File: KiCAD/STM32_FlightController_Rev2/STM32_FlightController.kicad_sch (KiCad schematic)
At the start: 71 parts, among them J1 USB_B_Micro, J11 GPS_V_{IN}, J12 GPS_TX, J13 GND, J14 GPS_RX, J15 ELRS_V_{IN}, J16 GND, J17 ELRS_TX, J18 ELRS_RX, J19 Conn_02x05_Odd_Even, J2 GND, J3 BAT, J4 CRT, J5 5V, J6 S1, J7 S2, J8 S3, J9 S4, Q1 IRLML6244, Q2 IRLML6244, SW1 PTS815SJM, SW2 SW_SPDT, U1 USBLC6-2SC6, U2 AMS1117-3.3, U3 TLV70018, U4 STM32F405RGTx, U5 BMP390L, U6 ICM-20948, Y1 8MHz

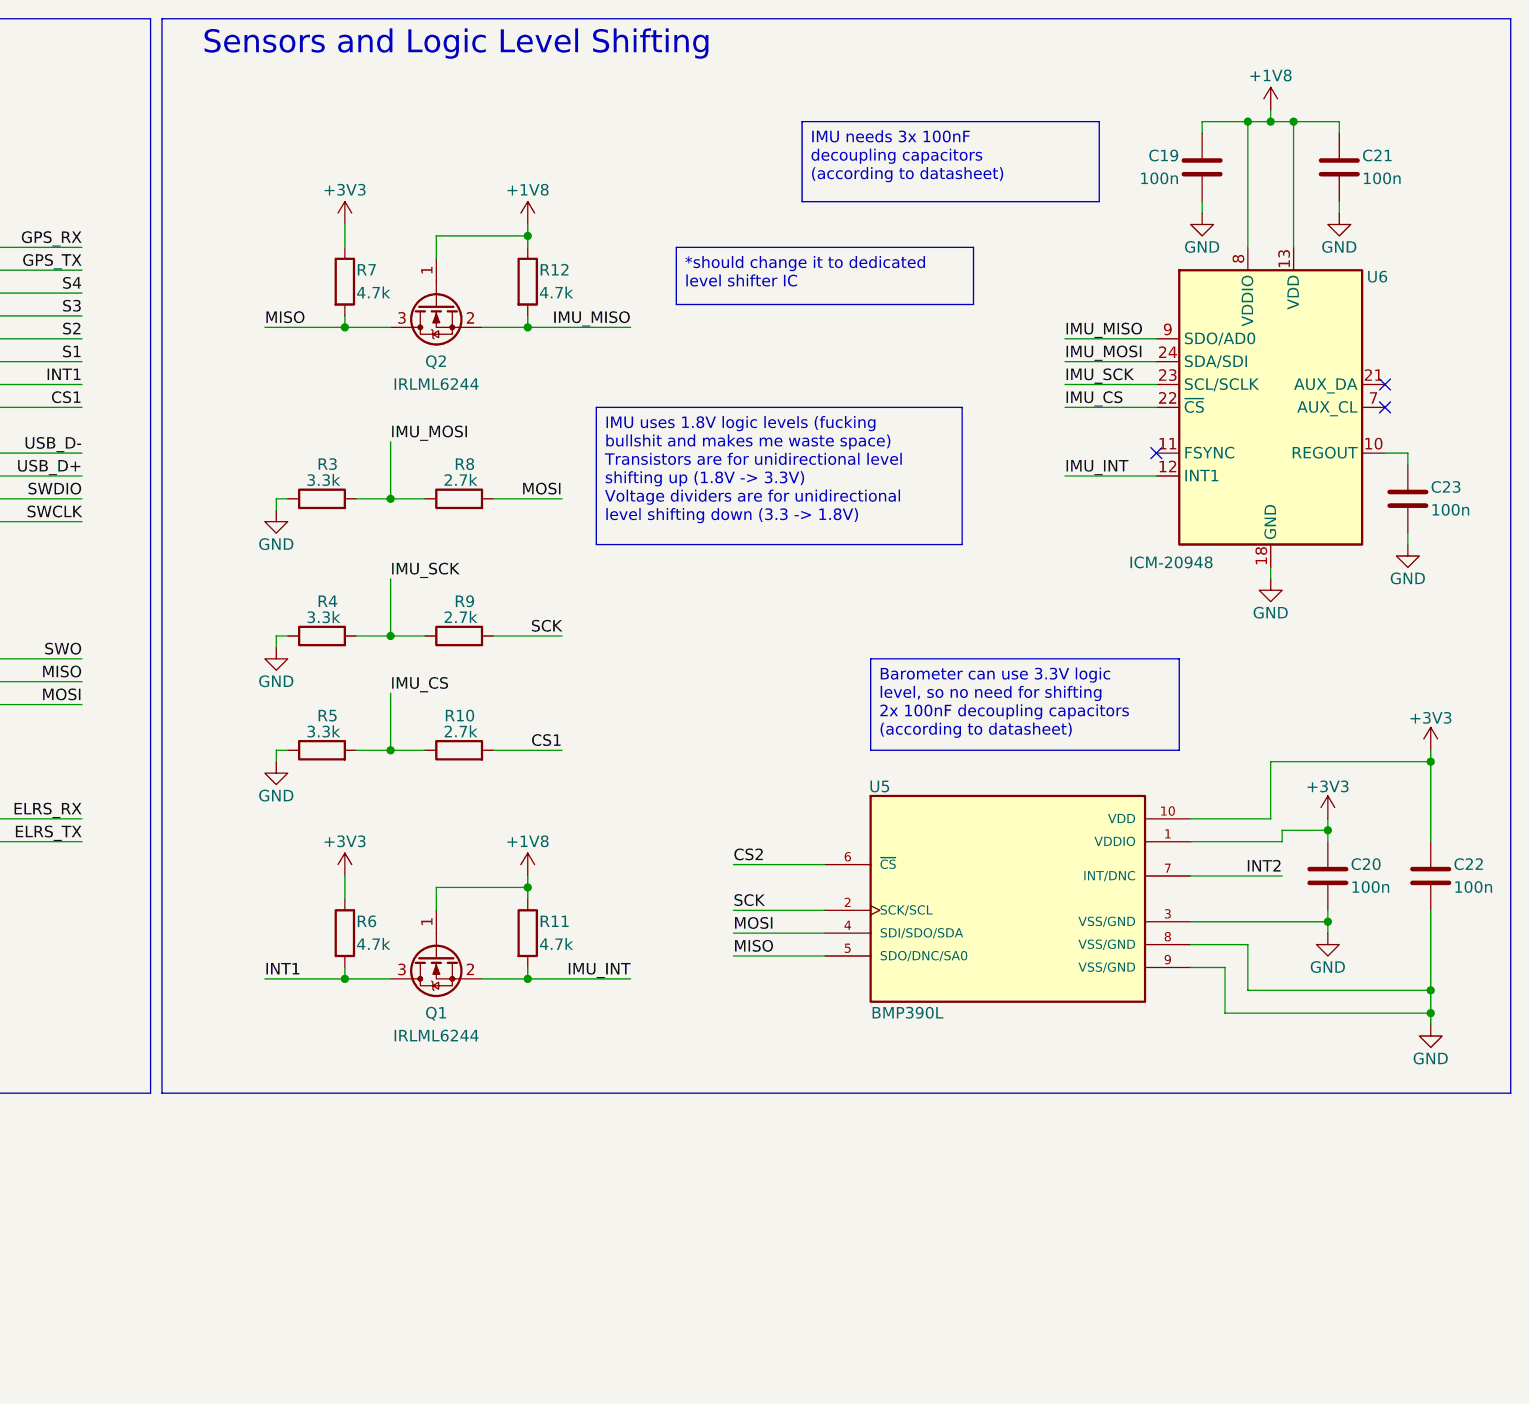
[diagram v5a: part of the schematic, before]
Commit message: replaced transistors with level shifter ICs
transistors appeared to switch to slowly for SPI, ICs seemed like they would be fast enough
required significant rerouting of SPI traces from sensors
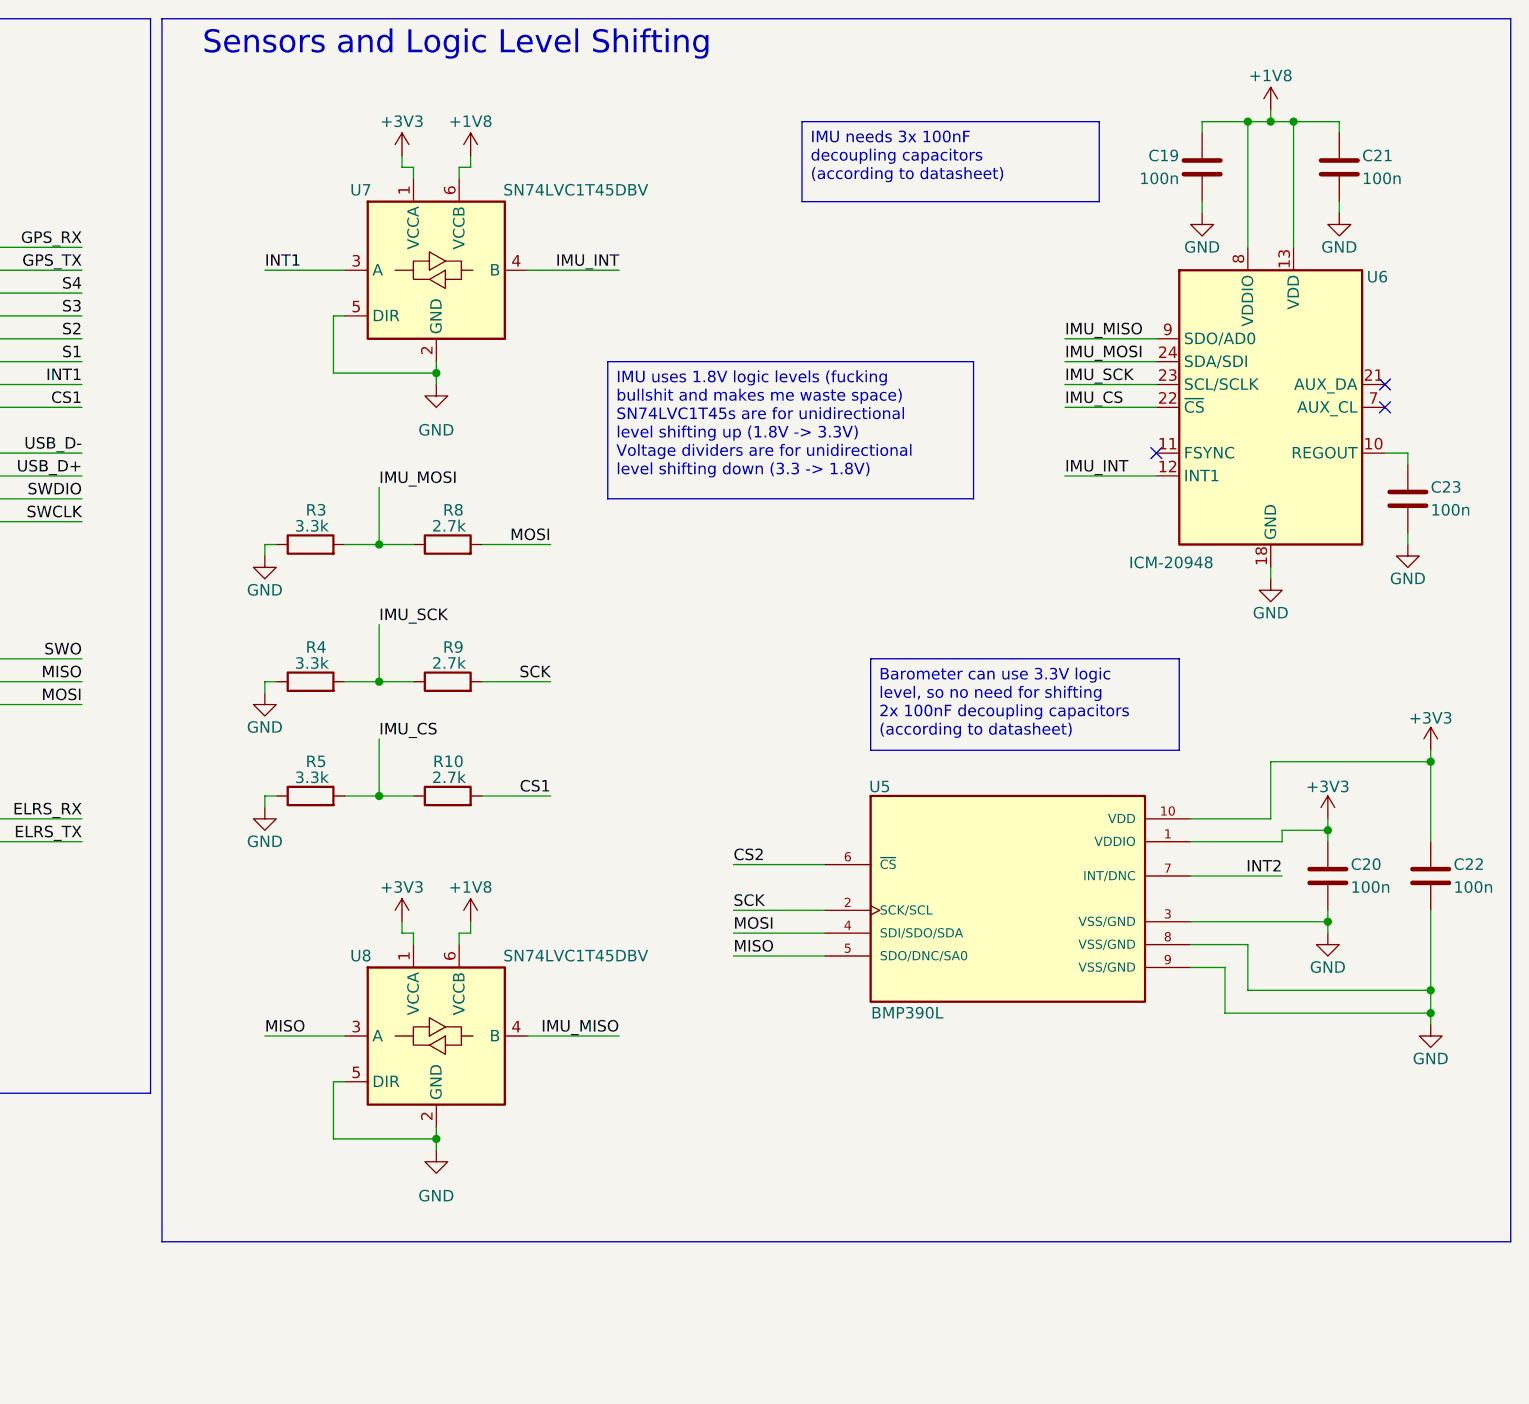
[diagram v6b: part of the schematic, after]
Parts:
- removed Q1, Q2: IRLML6244, Package_TO_SOT_SMD:SOT-23, symbol Transistor_FET:IRLML6244
- removed R11, R12, R6, R7: 4.7k, Resistor_SMD:R_0402_1005Metric, symbol Device:R
- added U7, U8: SN74LVC1T45DBV, Package_TO_SOT_SMD:SOT-23-6, symbol Logic_LevelTranslator:SN74LVC1T45DBV
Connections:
- net +1V8: now also U7.6 (VCCB), U8.6 (VCCB)
- net +3V3: now also U7.1 (VCCA), U8.1 (VCCA)
- net GND: now also U7.2 (GND), U7.5 (DIR), U8.2 (GND), U8.5 (DIR)
- net IMU_INT: now also U7.4 (B)
- net IMU_MISO: now also U8.4 (B)
- net INT1: now also U7.3 (A)
- net MISO: now also U8.3 (A)
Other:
- moved on the sheet: R10, R3, R4, R5, R8, R9

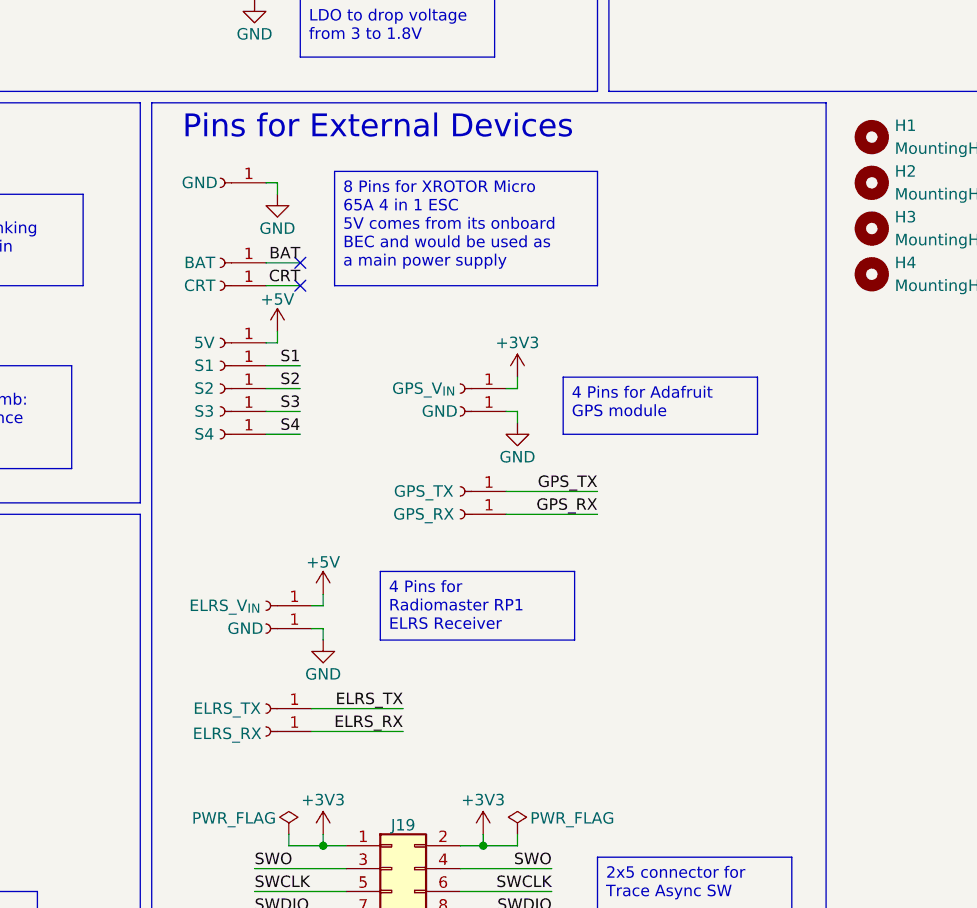
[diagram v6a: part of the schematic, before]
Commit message: replaced pads with corresponding JST-SH connectors
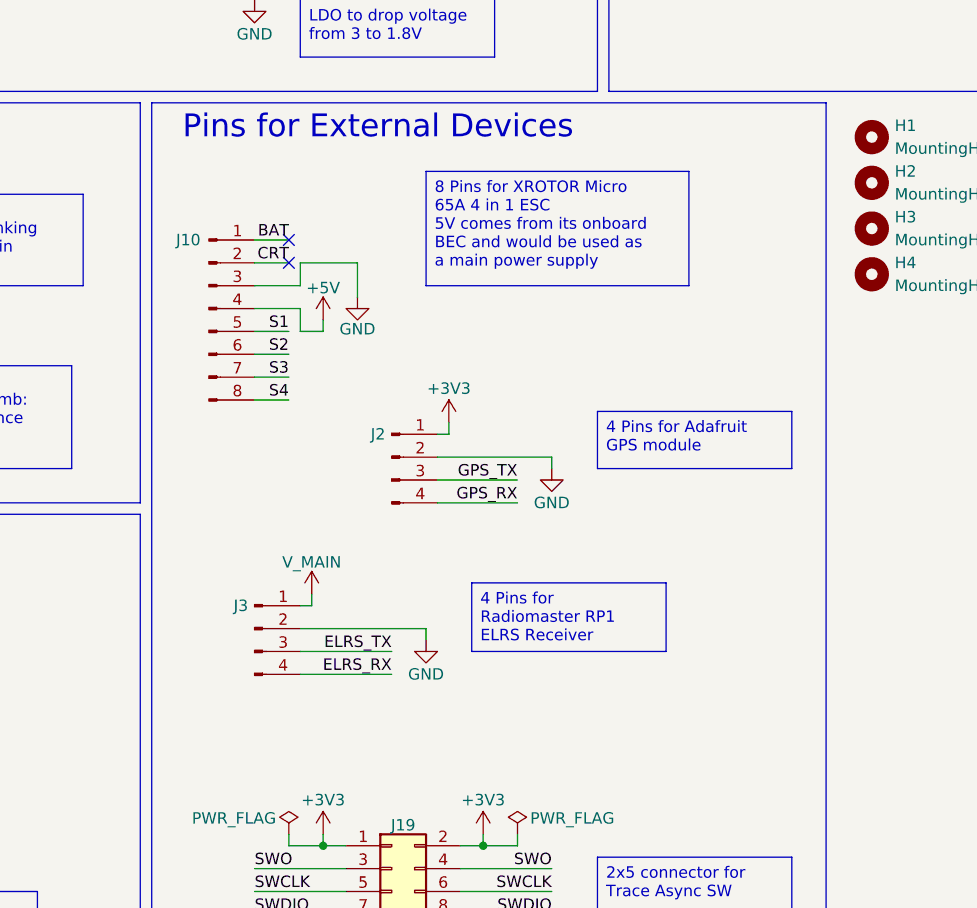
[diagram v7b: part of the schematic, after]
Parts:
- removed J11: GPS_V_{IN}, Connector_Wire:SolderWirePad_1x01_SMD_1x2mm, symbol Connector:Conn_01x01_Socket
- removed J12: GPS_TX, Connector_Wire:SolderWirePad_1x01_SMD_1x2mm, symbol Connector:Conn_01x01_Socket
- removed J13, J16, J2: GND, Connector_Wire:SolderWirePad_1x01_SMD_1x2mm, symbol Connector:Conn_01x01_Socket
- removed J14: GPS_RX, Connector_Wire:SolderWirePad_1x01_SMD_1x2mm, symbol Connector:Conn_01x01_Socket
- removed J15: ELRS_V_{IN}, Connector_Wire:SolderWirePad_1x01_SMD_1x2mm, symbol Connector:Conn_01x01_Socket
- removed J17: ELRS_TX, Connector_Wire:SolderWirePad_1x01_SMD_1x2mm, symbol Connector:Conn_01x01_Socket
- removed J18: ELRS_RX, Connector_Wire:SolderWirePad_1x01_SMD_1x2mm, symbol Connector:Conn_01x01_Socket
- removed J3: BAT, Connector_Wire:SolderWirePad_1x01_SMD_1x2mm, symbol Connector:Conn_01x01_Socket
- removed J4: CRT, Connector_Wire:SolderWirePad_1x01_SMD_1x2mm, symbol Connector:Conn_01x01_Socket
- removed J5: 5V, Connector_Wire:SolderWirePad_1x01_SMD_1x2mm, symbol Connector:Conn_01x01_Socket
- removed J6: S1, Connector_Wire:SolderWirePad_1x01_SMD_1x2mm, symbol Connector:Conn_01x01_Socket
- removed J7: S2, Connector_Wire:SolderWirePad_1x01_SMD_1x2mm, symbol Connector:Conn_01x01_Socket
- removed J8: S3, Connector_Wire:SolderWirePad_1x01_SMD_1x2mm, symbol Connector:Conn_01x01_Socket
- removed J9: S4, Connector_Wire:SolderWirePad_1x01_SMD_1x2mm, symbol Connector:Conn_01x01_Socket
- added J10: Conn_01x08_Pin, Connector_JST:JST_SH_SM08B-SRSS-TB_1x08-1MP_P1.00mm_Horizontal, symbol Connector:Conn_01x08_Pin
- added J2, J3: Conn_01x04_Pin, Connector_JST:JST_SH_SM04B-SRSS-TB_1x04-1MP_P1.00mm_Horizontal, symbol Connector:Conn_01x04_Pin
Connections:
- net +3V3: now also J2.1 (Pin_1)
- net +5V: now also J10.4 (Pin_4)
- net BAT: now also J10.1 (Pin_1)
- net CRT: now also J10.2 (Pin_2)
- net ELRS_RX: now also J3.4 (Pin_4)
- net ELRS_TX: now also J3.3 (Pin_3)
- net GND: now also J10.3 (Pin_3), J2.2 (Pin_2), J3.2 (Pin_2)
- net GPS_RX: now also J2.4 (Pin_4)
- net GPS_TX: now also J2.3 (Pin_3)
- net S1: now also J10.5 (Pin_5)
- net S2: now also J10.6 (Pin_6)
- net S3: now also J10.7 (Pin_7)
- net S4: now also J10.8 (Pin_8)
- net V_MAIN: now also J3.1 (Pin_1)

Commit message: finalizing components, adjusting some positioning
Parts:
- added R5, R8: 10k, Resistor_SMD:R_0402_1005Metric, symbol Device:R
- C21: renamed from C4; value 10p -> 14p
- C22: renamed from C7; value 10p -> 14p
- J1: value USB_B_Micro -> 629105150521
- J2: renamed from J10; value Conn_01x08_Pin -> JST_SH_SM08B-SRSS-TB_1x08-1MP_P1.00mm_Horizontal
- J3: renamed from J2; value Conn_01x04_Pin -> JST_SH_SM04B-SRSS-TB_1x04-1MP_P1.00mm_Horizontal
- J4: renamed from J3; value Conn_01x04_Pin -> JST_SH_SM04B-SRSS-TB_1x04-1MP_P1.00mm_Horizontal
- R1: renamed from R3; value 3.3k -> 3k3
- R2: renamed from R8; value 2.7k -> 2k7
- R3: renamed from R4; value 3.3k -> 2k7
- R4: renamed from R9; value 2.7k -> 2k7
- R6: renamed from R5; value 3.3k -> 3k3
- R7: renamed from R10; value 2.7k -> 2k7
- SW1: value PTS815SJM -> PTS815SJM250SMTRLFS
- SW2: value SW_SPDT -> PCM12SMTR
- Y1: value 8MHz -> X32258MOB4SI
- renumbered C19 to C10, C21 to C11, C23 to C12, C16 to C13, C17 to C14, C20 to C15, C22 to C16, C3 to C17, C9 to C18, C2 to C19, C5 to C2, C11 to C20, C8 to C23, C6 to C3, C10 to C4, C12 to C5, C13 to C6, C14 to C7, C15 to C8, C18 to C9, D2 to D1, D1 to D2, J19 to J5, R1 to R10, R2 to R9, U7 to U1, U6 to U2, U4 to U3, U1 to U4, U2 to U5, U3 to U6, U5 to U7
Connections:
- net +3V3: now also R5.2, R8.2
- net CS1: now also R5.1
- net CS2: now also R8.1
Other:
- moved on the sheet: C10, C11, C12, C23, R10, SW1, SW2, U2
